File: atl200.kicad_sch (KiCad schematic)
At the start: 0 parts

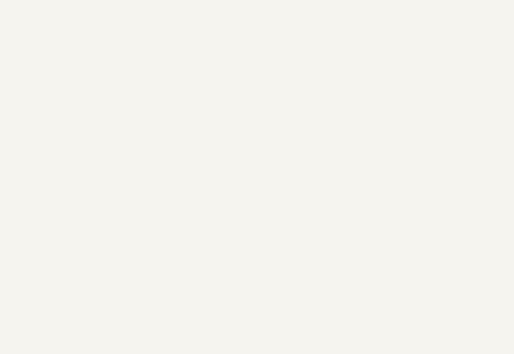
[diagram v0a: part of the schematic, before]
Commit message: feat: Create a Mini PCI Express (mPCI Express) interface #3
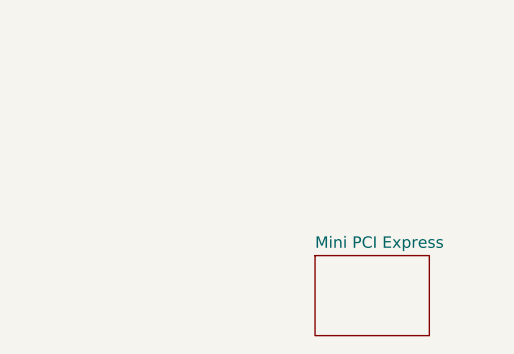
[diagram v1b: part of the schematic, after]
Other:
- added sheet Mini PCI Express (atl200_mpcie.kicad_sch)
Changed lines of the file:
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@@
 	(title_block
 		(title "ATL-200 (Multiparametric Station)")
-		(date "2025-06-08")
+		(date "2025-06-09")
 		(rev "v0.1.0")
 		(company "AgroTechLab (Agribusiness Technology Development Laboratory)")
@@
 		)
 	)
+	(sheet
+		(at 181.61 149.86)
+		(size 12.7 8.89)
+		(exclude_from_sim no)
+		(in_bom yes)
+		(on_board yes)
+		(dnp no)
+		(fields_autoplaced yes)
+		(stroke
+			(width 0.1524)
+			(type solid)
+		)
+		(fill
+			(color 0 0 0 0.0000)
+		)
+		(property "Sheetname" "Mini PCI Express"
+			(at 181.61 149.1484 0)
+			(effects
+				(font
+					(size 1.27 1.27)
+				)
+				(justify left bottom)
+			)
+		)
+		(property "Sheetfile" "atl200_mpcie.kicad_sch"
+			(at 181.61 159.3346 0)
+			(effects
+				(font
+					(size 1.27 1.27)
+				)
+				(justify left top)
+				(hide yes)
+			)
+		)
+		(instances
+			(project "atl200"
+				(path "/70f4b7a7-bc92-4e08-aa87-1db70636b26b"
+					(page "2")
+				)
+			)
+		)
+	)
